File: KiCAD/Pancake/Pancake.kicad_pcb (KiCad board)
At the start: 2 copper layers, 215.9 x 142.2 mm, 201 parts, among them IC10 LF347N, IC3 LF347N, IC4 LF347N, IC5 LF347N, IC6 LF347N, IC7 LF347N, IC8 LF347N, IC9 LF347N, J1 Conn_01x08_Male, J101 TB001-500-04BE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

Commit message: Revising one last time before ordering
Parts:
- added R89: 1000, Resistor_SMD:R_1206_3216Metric_Pad1.30x1.75mm_HandSolder, F.Cu at (232.9, 39.1)
- R87: value 500 -> 1000
- moved R87 1.75 mm to (227.3, 39.1)
- moved LED1 1.27 mm to (230.2, 35.1)
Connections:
- R87 pad 1: Net-(LED1-Pad2) -> +12V
- R87 pad 2: +12V -> Net-(LED1-Pad2)
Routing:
- net +12V: track 563.9 -> 574.7 mm
- net Net-(LED1-Pad2): track 5.33 -> 10.9 mm

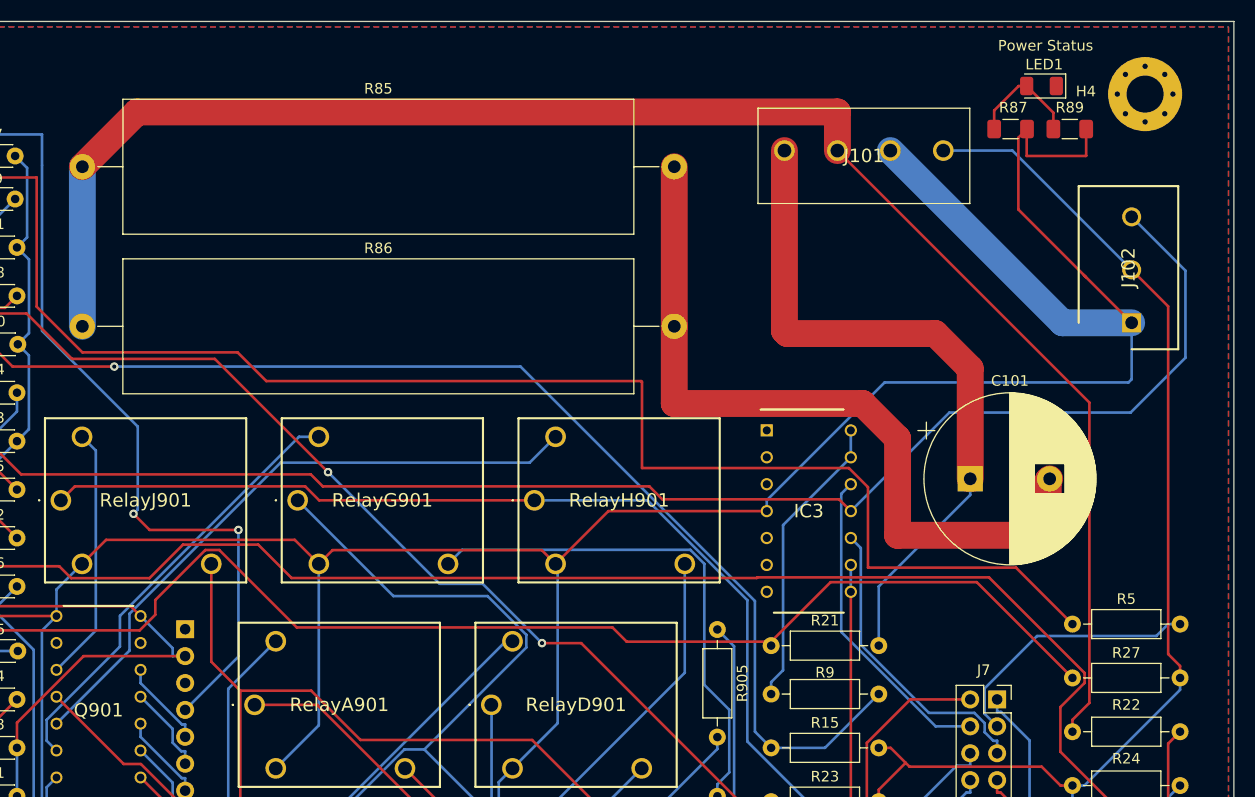
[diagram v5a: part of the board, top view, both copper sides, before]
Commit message: Moving trace to keep antenna effect low
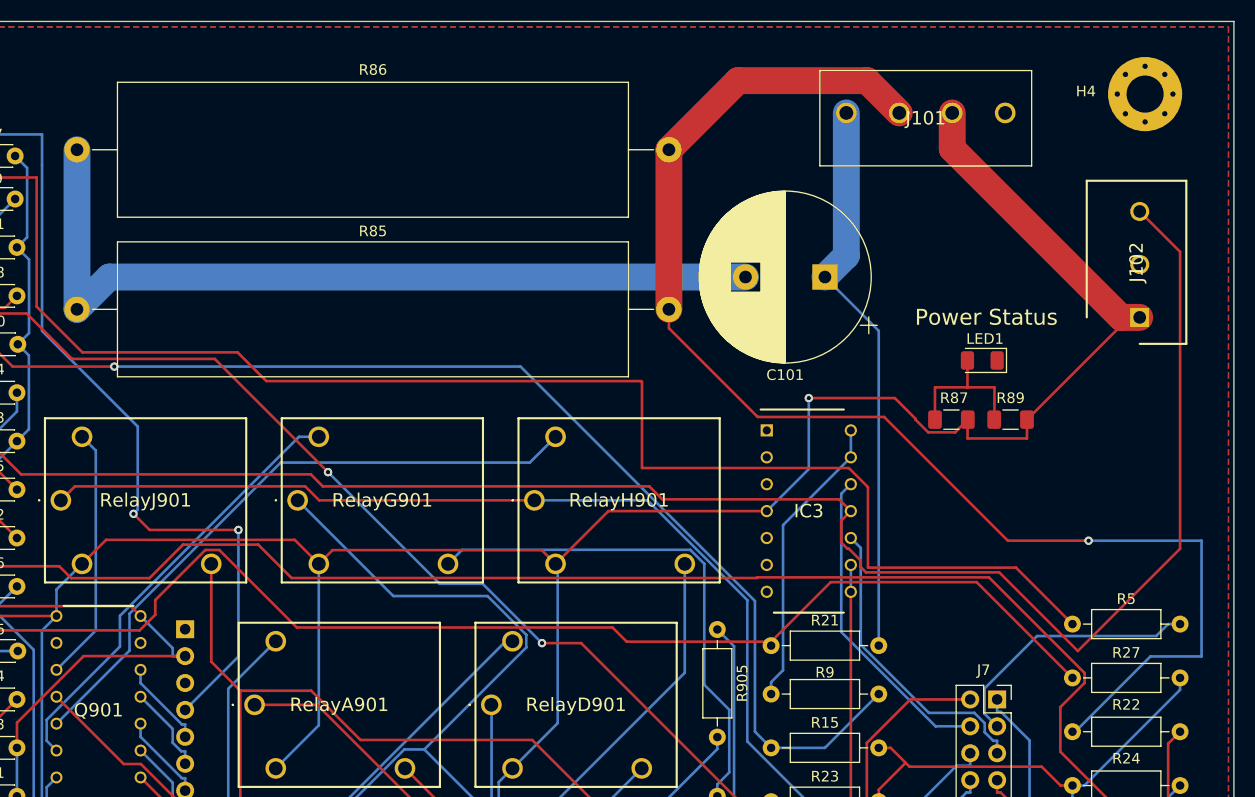
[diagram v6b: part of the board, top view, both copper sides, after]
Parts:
- moved R86 57.8 mm to (195.1, 41.1), turned to 180 degrees
- moved R85 57.0 mm to (195.1, 56.1), turned to 180 degrees
- moved R87 28.0 mm to (221.7, 66.5)
- moved R89 28.0 mm to (227.3, 66.5)
- moved LED1 26.5 mm to (224.7, 61.0)
- moved C101 23.5 mm to (209.8, 53.1), turned to 180 degrees
- moved J101 6.84 mm to (226.8, 37.6)
- moved J102 0.92 mm to (239.5, 56.9)
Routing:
- net GND: track 756.5 -> 693.7 mm
- net /SPRKNeg: track 157.5 -> 127.2 mm, vias 0 -> 1
- net +12V: track 574.7 -> 546.3 mm, vias 0 -> 1
- net -12V: track 314.7 -> 338.7 mm
- net /SPRKPos: track 65.8 -> 53.2 mm
- net Net-(C101-Pad2): track 73.6 -> 79.4 mm
- net Net-(LED1-Pad2): track 10.9 -> 14.2 mm

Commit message: Test
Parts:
- C12, C22, C32, C42, C52, C62, C72: value 180nF -> 180pF
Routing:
- net GND: track 693.7 -> 850.8 mm, vias 0 -> 26
- net Net-(Q901-Pad12): track 64.1 -> 65.6 mm
- net (no net): vias 0 -> 2

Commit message: Give it a look, then let blow the horn.
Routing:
- net GND: track 850.8 -> 895.3 mm, vias 26 -> 121
- net /12VOut: track 141.4 -> 143.5 mm
- net /GuitarIn: track 159.0 -> 161.0 mm
- net /ADC89/IN2: track 274.6 -> 276.4 mm
- net Net-(C61-Pad1): track 39.3 -> 40.5 mm
- net (no net): vias 2 -> 0
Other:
- board text added: "A"
